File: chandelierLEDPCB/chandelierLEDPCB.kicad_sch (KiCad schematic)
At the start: 10 parts, among them J1 JST PH 1x02 SMT VERT, J3 JST PH 1x02 SMT VERT

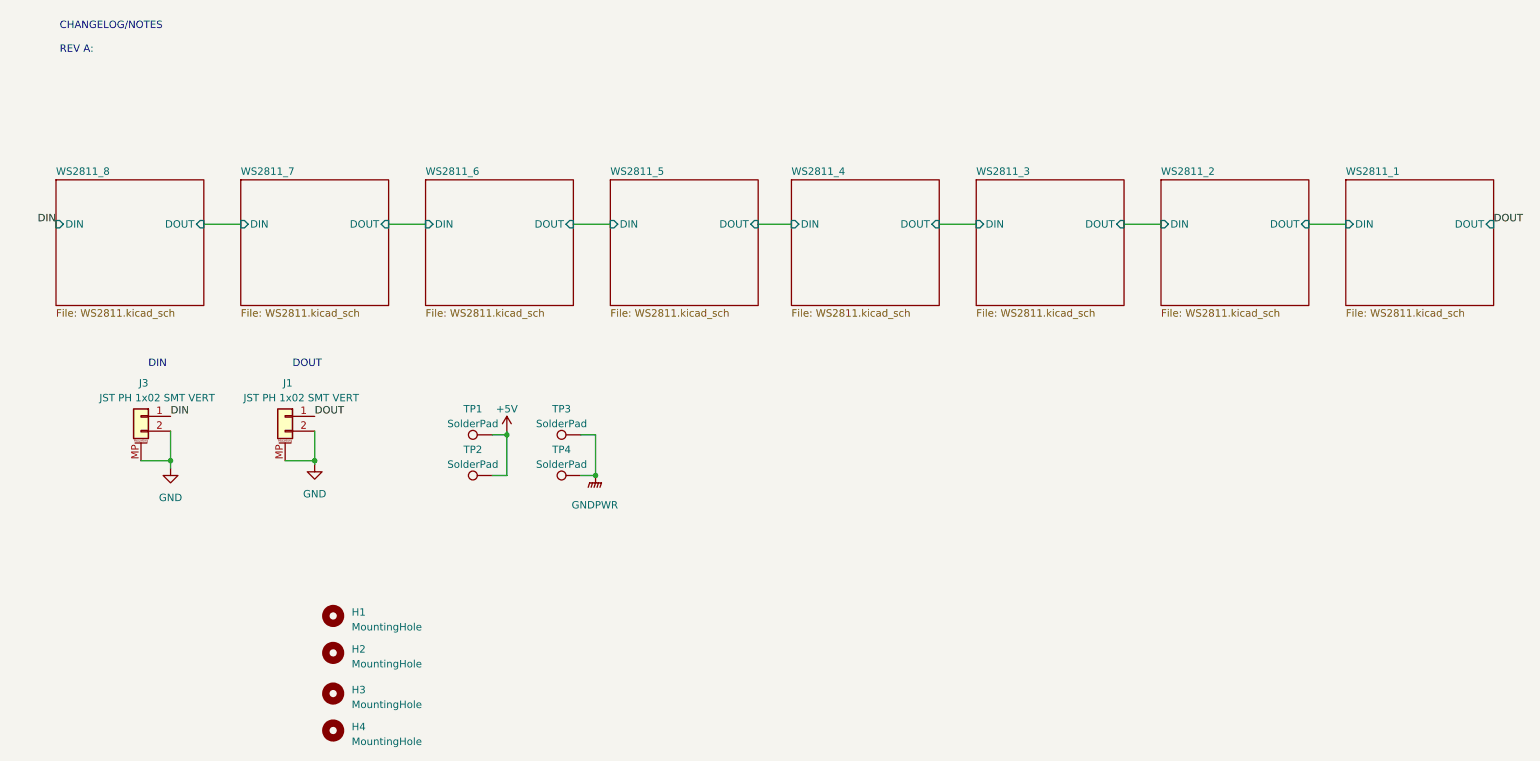
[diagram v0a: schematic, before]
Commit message: updated schematic to include rev, edited sheet size
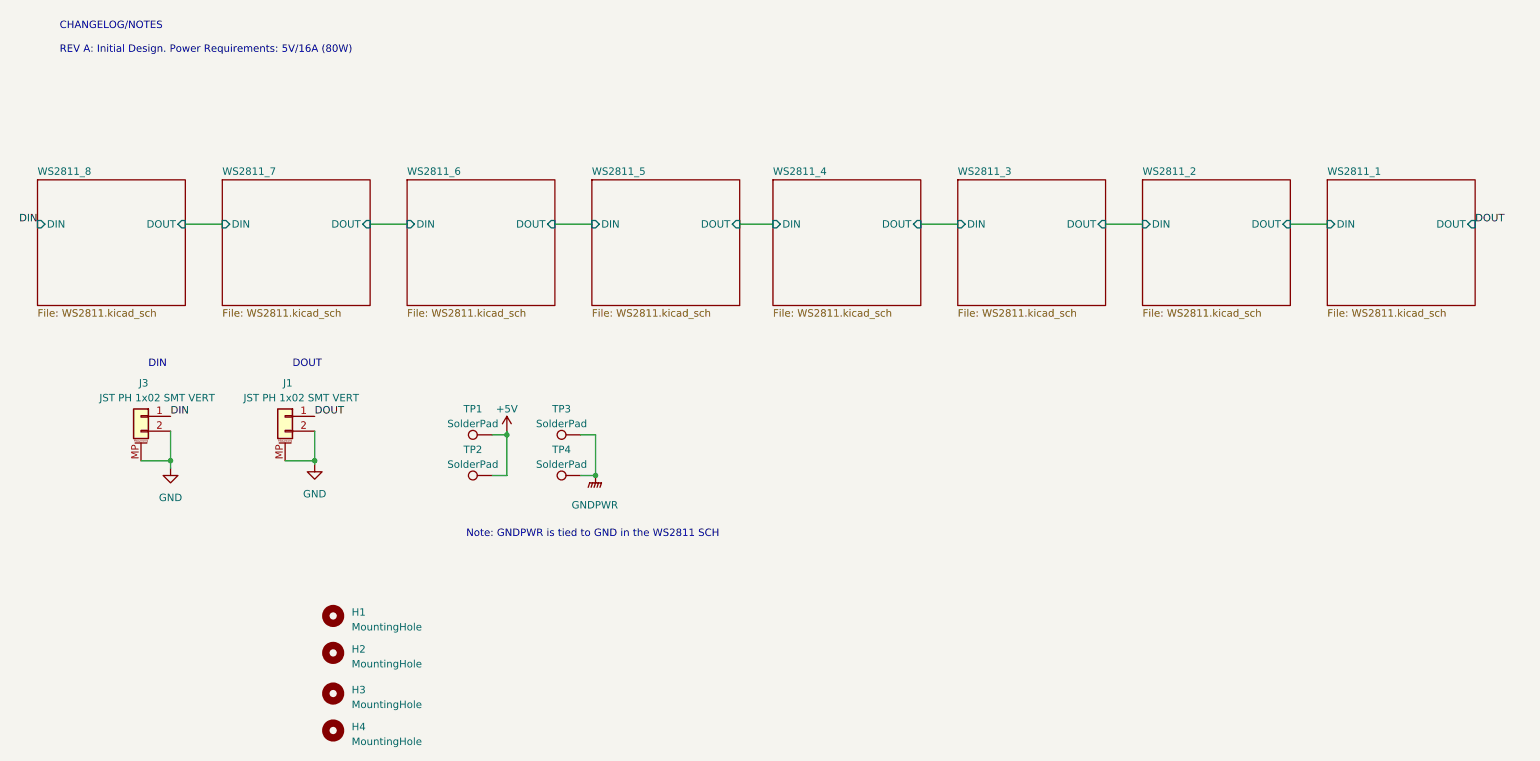
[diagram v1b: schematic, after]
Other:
- note added: "CHANGELOG/NOTES REV A: Initial Design. Power Requirements: 5V/16A (80W)"
- note added: "Note: GNDPWR is tied to GND in the WS2811 SCH"
- note removed: "CHANGELOG/NOTES REV A:"

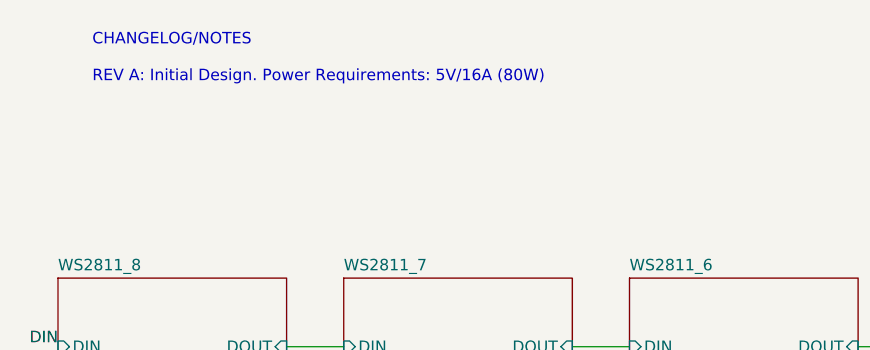
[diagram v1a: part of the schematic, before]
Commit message: Edited LED to have EP disconnected
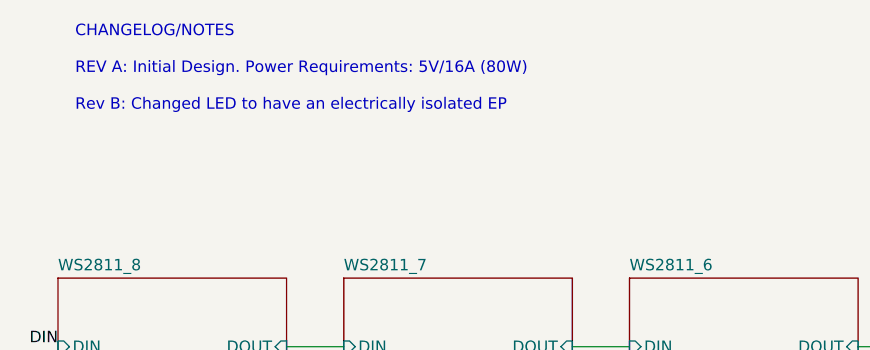
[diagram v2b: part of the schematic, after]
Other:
- note added: "CHANGELOG/NOTES REV A: Initial Design. Power Requirements: 5V/16A (80W) Rev B: Changed LED to have an electrically isolated EP"
- note removed: "CHANGELOG/NOTES REV A: Initial Design. Power Requirements: 5V/16A (80W)"
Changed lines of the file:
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@@
   (title_block
     (title "Main")
-    (date "2023-04-08")
-    (rev "A01")
+    (date "2023-04-24")
+    (rev "B01")
   )
   (junction (at 111.76 95.25) (diameter 0) (color 0 0 0 0)
@@
     (effects (font (size 1.27 1.27)) (justify left bottom))
   )
-  (text "CHANGELOG/NOTES\n\nREV A: Initial Design. Power Requirements: 5V/16A (80W)"
-    (at 19.685 22.86 0)
+  (text "CHANGELOG/NOTES\n\nREV A: Initial Design. Power Requirements: 5V/16A (80W)\n\nRev B: Changed LED to have an electrically isolated EP"
+    (at 17.78 26.035 0)
     (effects (font (size 1.27 1.27)) (justify left bottom))
   )
